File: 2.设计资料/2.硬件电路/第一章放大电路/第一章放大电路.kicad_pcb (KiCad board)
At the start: 2 copper layers, 110 parts, among them J1 VIN_15V, J10 Vout4-, J11 Vout4+, J12 Vout5, J13 Vin_sin7, J14 Vin_sin6, J15 Vin_sin8, J16 Vout7, J17 Vout6, J18 Vout8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

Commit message: PCB 布局完成
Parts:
- D1: value D_Small -> 1N4148
- moved J17 234.2 mm to (37.0, 81.0), turned to 180 degrees
- moved Q7 224.8 mm to (28.0, 76.0)
- moved J14 217.7 mm to (20.0, 78.5)
- moved J18 211.6 mm to (67.0, 61.0), turned to 180 degrees
- moved Q8 205.0 mm to (58.0, 56.2)
- moved J15 195.7 mm to (50.0, 58.5)
- moved R4 185.4 mm to (27.0, 61.1), turned to 270 degrees
- moved C36 183.3 mm to (33.0, 81.1), turned to 90 degrees
- moved C45 182.7 mm to (33.0, 71.1), turned to 90 degrees
- moved C32 172.1 mm to (24.0, 81.1), turned to 270 degrees
- moved R25 169.4 mm to (24.0, 71.1), turned to 270 degrees
- moved R14 168.5 mm to (54.0, 81.1), turned to 270 degrees
- moved R30 165.5 mm to (27.0, 71.1), turned to 270 degrees
- moved J16 164.3 mm to (105.0, 41.0), turned to 180 degrees
- moved Q6 163.7 mm to (96.0, 36.0)
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
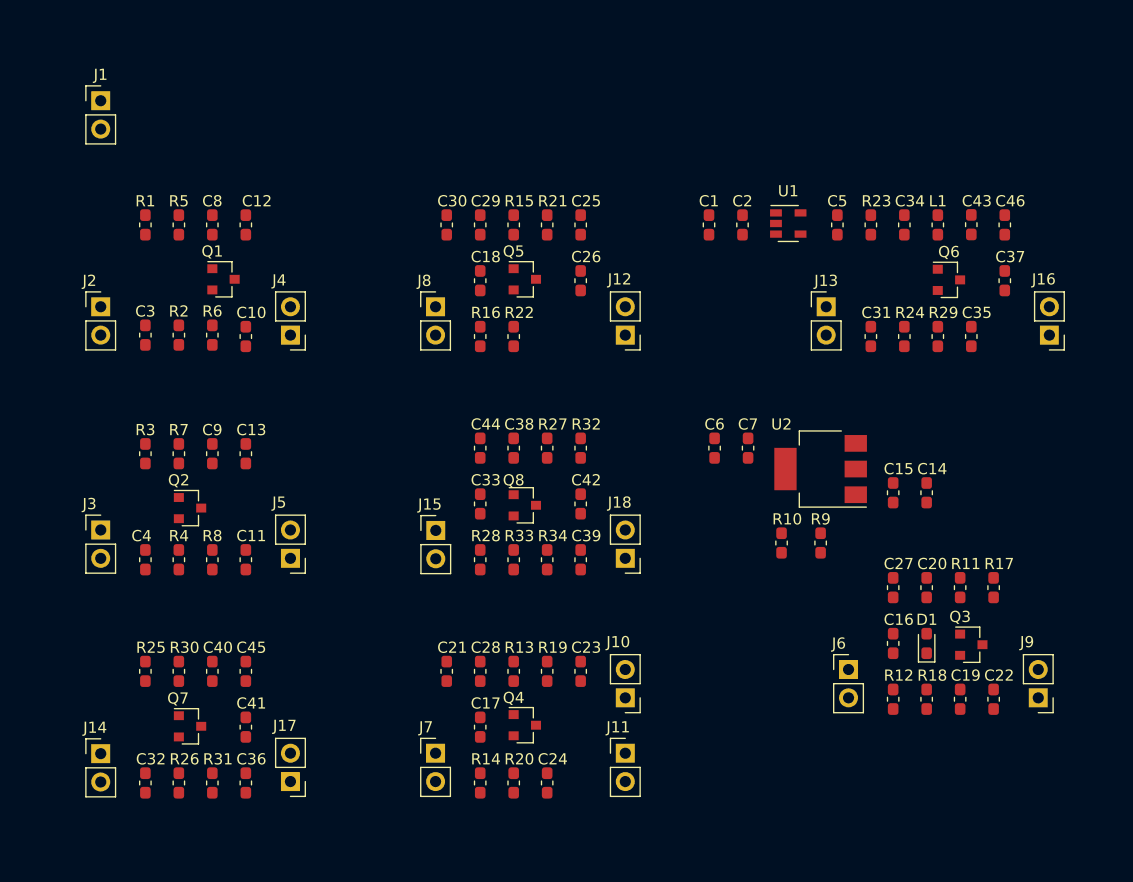
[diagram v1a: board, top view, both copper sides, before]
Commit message: PCB布板完成，并且生成gerber文件
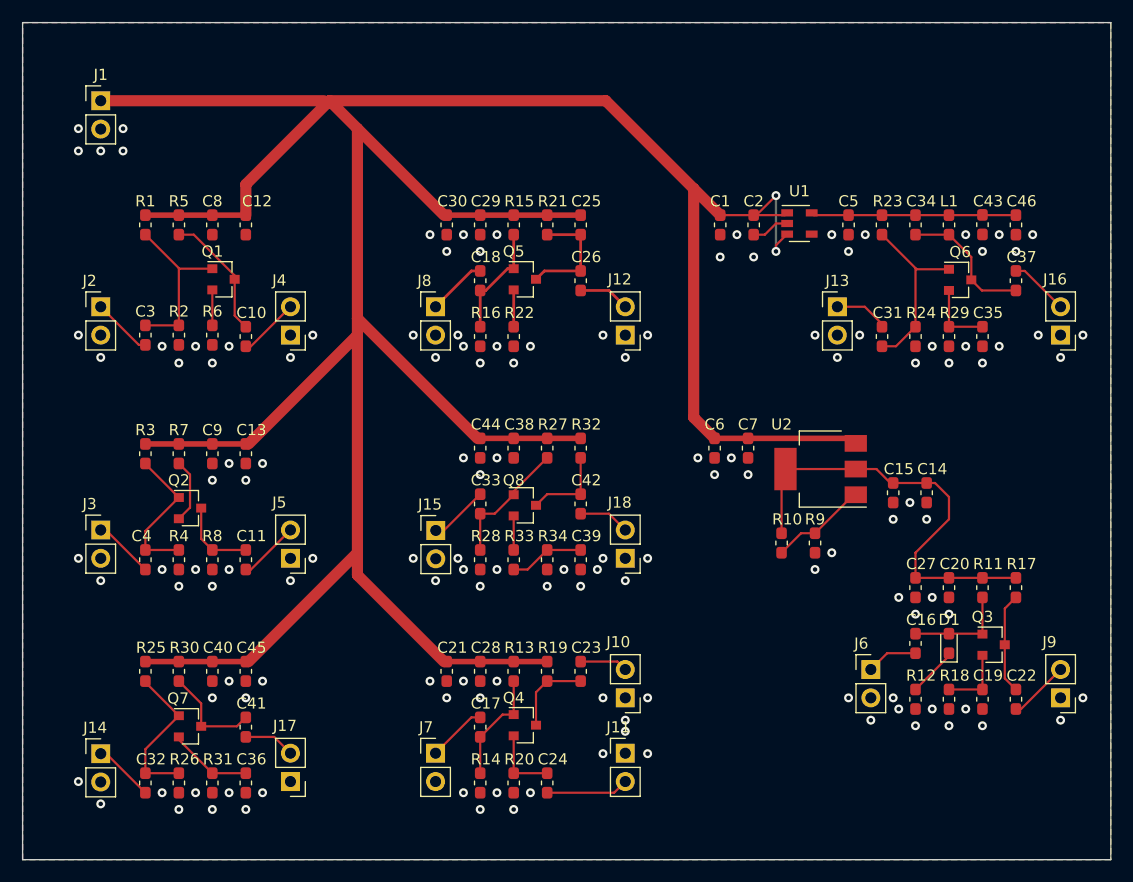
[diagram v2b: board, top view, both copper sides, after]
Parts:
- moved C16 2.00 mm to (93.0, 68.6)
- moved C19 2.00 mm to (99.0, 73.6)
- moved C20 2.00 mm to (96.0, 63.6)
- moved C22 2.00 mm to (102.0, 73.6)
- moved C27 2.00 mm to (93.0, 63.6)
- moved D1 2.00 mm to (96.0, 68.6)
- moved J6 2.00 mm to (89.0, 71.0)
- moved J9 2.00 mm to (106.0, 73.5)
- moved Q3 2.00 mm to (100.0, 68.7)
- moved R11 2.00 mm to (99.0, 63.6)
- moved R12 2.00 mm to (93.0, 73.6)
- moved R17 2.00 mm to (102.0, 63.6)
- moved R18 2.00 mm to (96.0, 73.6)
- moved C1 1.00 mm to (75.5, 31.1)
- moved C2 1.00 mm to (78.5, 31.1)
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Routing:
- net +15V: track 0.00 -> 291.3 mm, vias 0 -> 2
- net +1V5: track 0.00 -> 39.1 mm
- net +4V: track 0.00 -> 18.4 mm
- net Net-(C31-Pad1): track 0.00 -> 16.3 mm
- net Net-(C3-Pad1): track 0.00 -> 15.4 mm
- net Net-(C32-Pad1): track 0.00 -> 13.7 mm
- net Net-(C4-Pad1): track 0.00 -> 13.2 mm
- net Net-(C34-Pad1): track 0.00 -> 12.3 mm
- net Net-(C10-Pad2): track 0.00 -> 11.5 mm
- net Net-(C33-Pad1): track 0.00 -> 11.5 mm
- net Net-(C25-Pad1): track 0.00 -> 10.6 mm
- net Net-(C18-Pad1): track 0.00 -> 10.1 mm
- net Net-(C17-Pad1): track 0.00 -> 10.1 mm
- net Net-(C16-Pad1): track 0.00 -> 9.31 mm
- net Net-(C41-Pad2): track 0.00 -> 9.21 mm
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- added copper zone on B.Cu, net GND
- added copper zone on F.Cu, net GND
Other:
- board outline added: 97.5 x 75 mm
